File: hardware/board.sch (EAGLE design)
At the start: 45 parts, among them IC1 0915BM15A0001, J1 U.FL, U3 BLE113-A, X1 26MHz 10pF 10ppm -20C +70C, X3 MINI-USB-UX60-MB-5ST

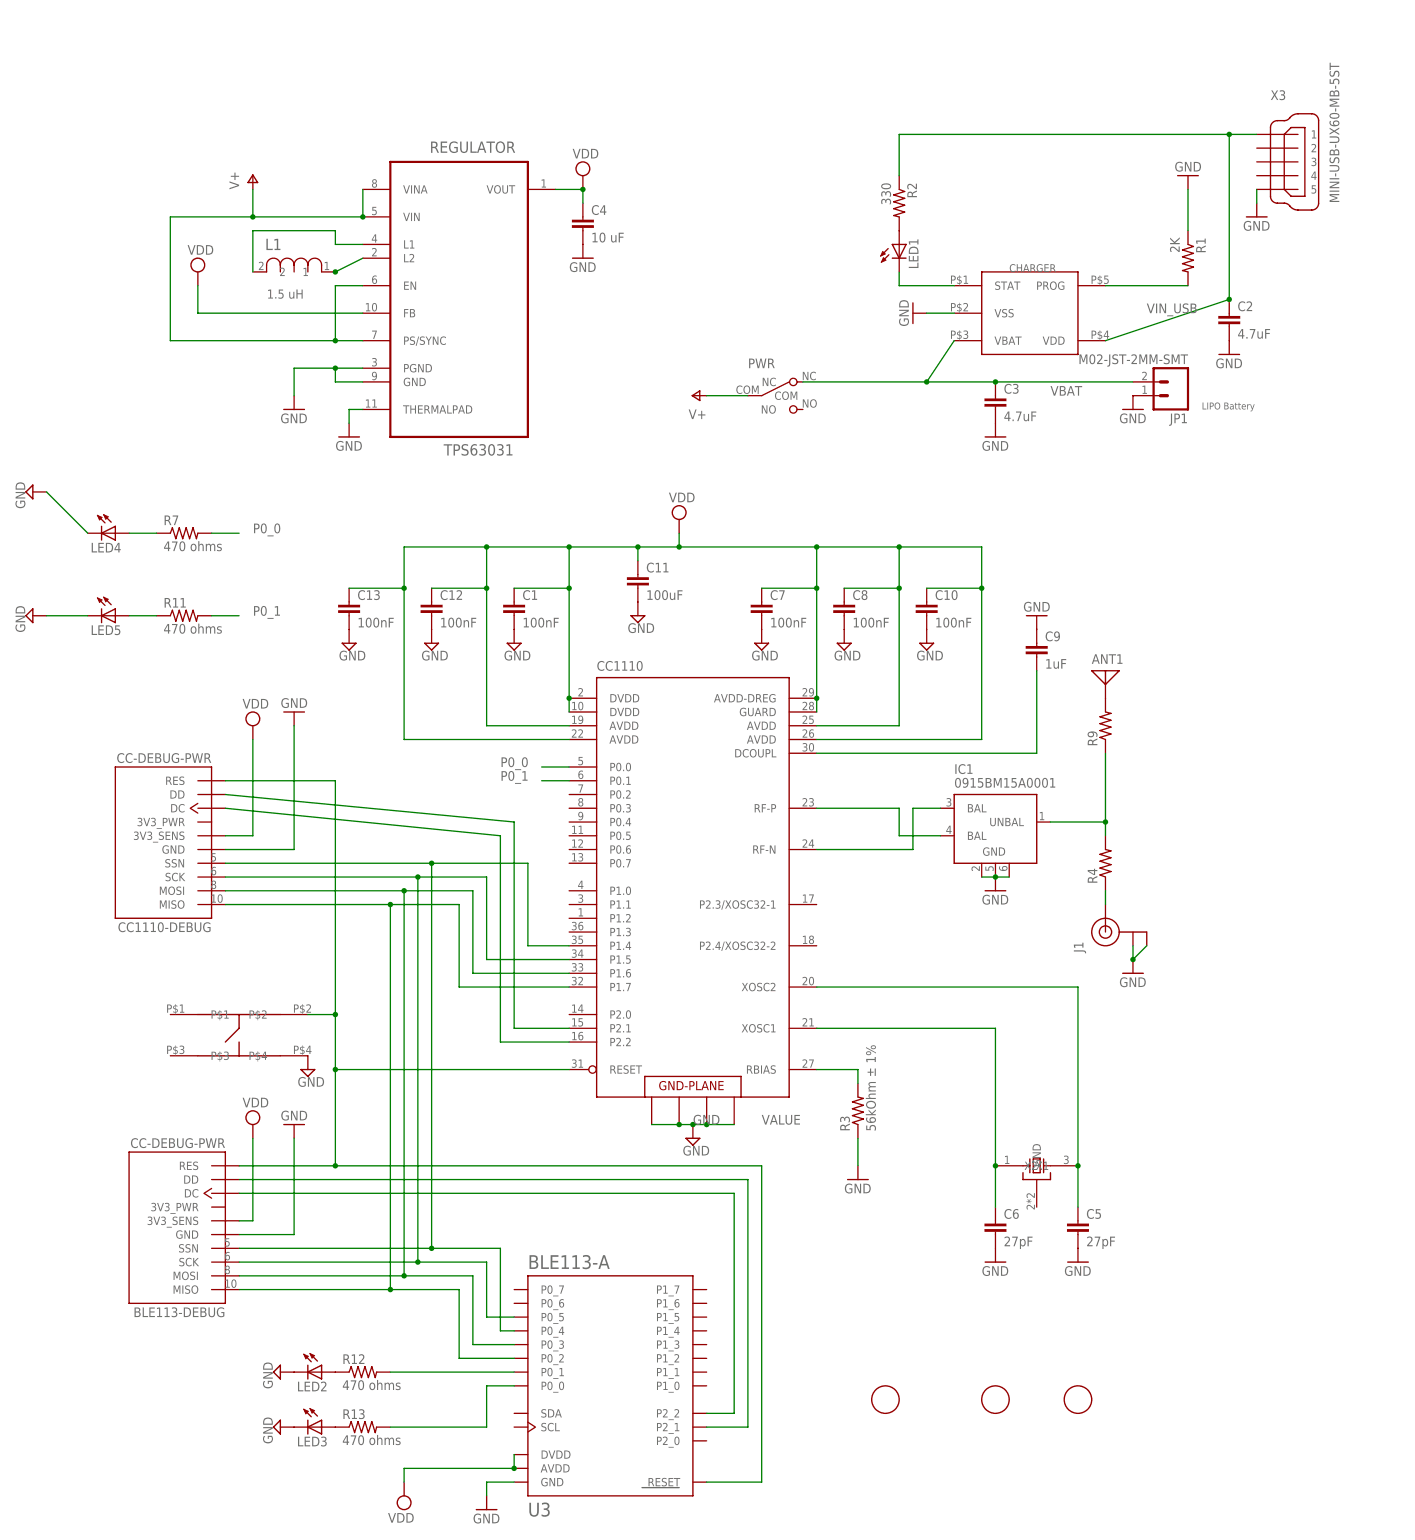
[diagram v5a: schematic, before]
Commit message: Add colors to leds, and switch 4.7uF cap from 0402 to 0603 package
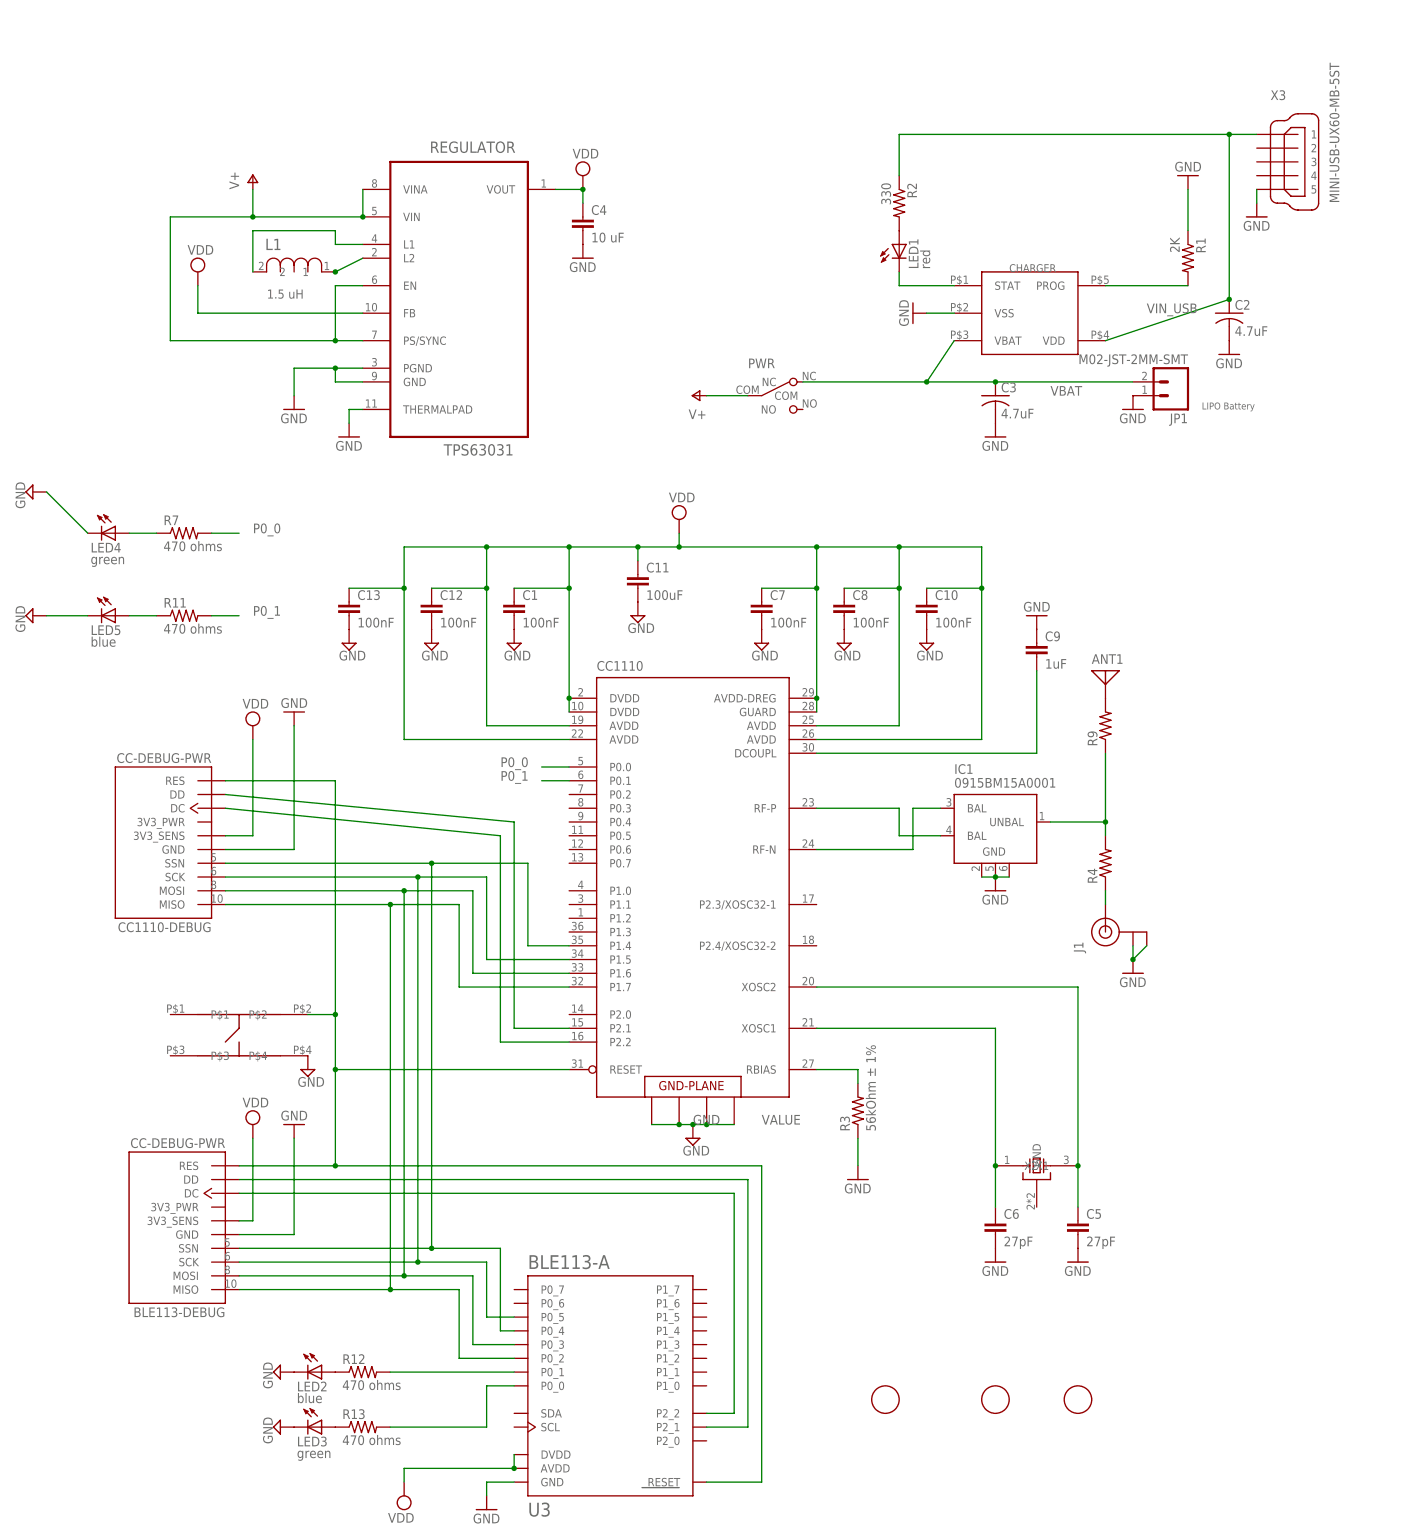
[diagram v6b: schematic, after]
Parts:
- C2: device rcl:C-EUC0402K -> rcl:C-USC0603K
- C3: device rcl:C-EUC0603K -> rcl:C-USC0603K
- LED1: value (none) -> red
- LED2, LED5: value (none) -> blue
- LED3, LED4: value (none) -> green
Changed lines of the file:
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@@
 <part name="JP1" library="SparkFun-Connectors" deviceset="M02" device="-JST-2MM-SMT"/>
 <part name="GND1" library="supply1" deviceset="GND" device=""/>
-<part name="C2" library="rcl" deviceset="C-EU" device="C0402K" value="4.7uF"/>
+<part name="C2" library="rcl" deviceset="C-US" device="C0603K" value="4.7uF"/>
 <part name="GND3" library="supply1" deviceset="GND" device=""/>
 <part name="R1" library="rcl" deviceset="R-US_" device="R0402" value="2K"/>
 <part name="R2" library="rcl" deviceset="R-US_" device="R0402" value="330"/>
-<part name="LED1" library="led" deviceset="LED" device="SML0603"/>
+<part name="LED1" library="led" deviceset="LED" device="SML0603" value="red"/>
 <part name="GND2" library="supply1" deviceset="GND" device=""/>
 <part name="GND4" library="supply1" deviceset="GND" device=""/>
-<part name="C3" library="rcl" deviceset="C-EU" device="C0603K" value="4.7uF"/>
+<part name="C3" library="rcl" deviceset="C-US" device="C0603K" value="4.7uF"/>
 <part name="GND5" library="supply1" deviceset="GND" device=""/>
 <part name="GND6" library="supply1" deviceset="GND" device=""/>
@@
 <part name="R11" library="rcl" deviceset="R-US_" device="R0402" value="470 ohms"/>
 <part name="SUPPLY10" library="supply2" deviceset="GND" device=""/>
-<part name="LED4" library="led" deviceset="LED" device="SML0603"/>
-<part name="LED5" library="led" deviceset="LED" device="SML0603"/>
+<part name="LED4" library="led" deviceset="LED" device="SML0603" value="green"/>
+<part name="LED5" library="led" deviceset="LED" device="SML0603" value="blue"/>
 <part name="SUPPLY11" library="supply2" deviceset="GND" device=""/>
 <part name="SUPPLY12" library="supply2" deviceset="GND" device=""/>
-<part name="LED2" library="led" deviceset="LED" device="SML0603"/>
+<part name="LED2" library="led" deviceset="LED" device="SML0603" value="blue"/>
 <part name="R12" library="rcl" deviceset="R-US_" device="R0402" value="470 ohms"/>
 <part name="SUPPLY13" library="supply2" deviceset="GND" device=""/>
-<part name="LED3" library="led" deviceset="LED" device="SML0603"/>
+<part name="LED3" library="led" deviceset="LED" device="SML0603" value="green"/>
 <part name="R13" library="rcl" deviceset="R-US_" device="R0402" value="470 ohms"/>
 <part name="C7" library="rcl" deviceset="C-EU" device="C0402" value="100nF"/>

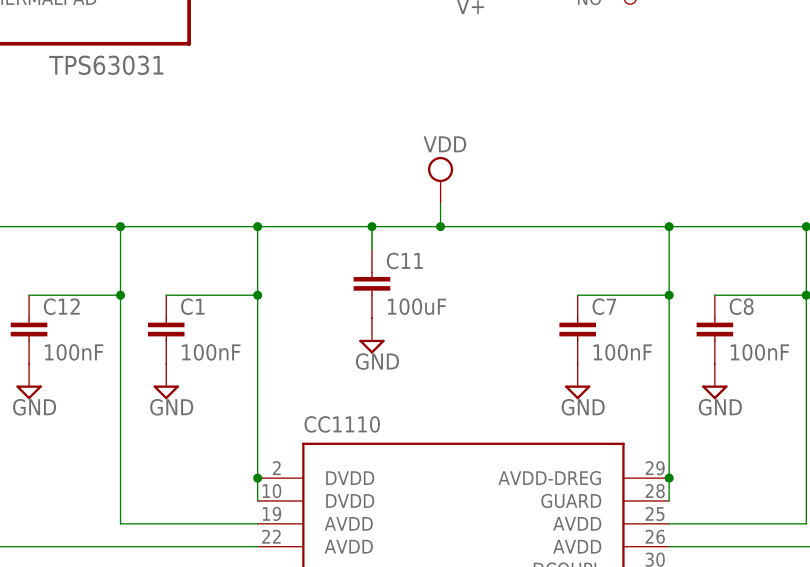
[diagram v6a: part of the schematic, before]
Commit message: Update C11 to 0805
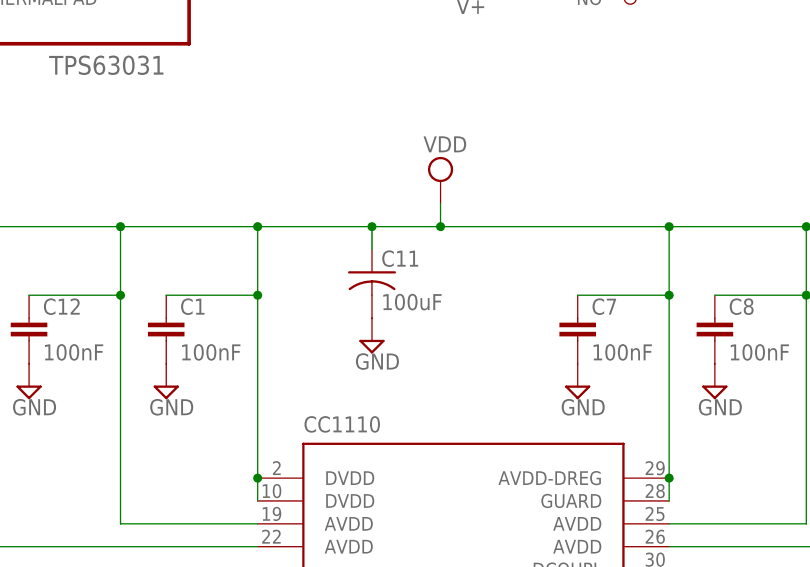
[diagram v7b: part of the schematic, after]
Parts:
- C11: device rcl:C-EUC0402 -> rcl:C-USC0805K
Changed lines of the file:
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@@
 <part name="SUPPLY19" library="supply2" deviceset="GND" device=""/>
 <part name="SUPPLY20" library="supply2" deviceset="GND" device=""/>
-<part name="C11" library="rcl" deviceset="C-EU" device="C0402" value="100uF"/>
+<part name="C11" library="rcl" deviceset="C-US" device="C0805K" value="100uF"/>
 <part name="SUPPLY15" library="supply2" deviceset="GND" device=""/>
 <part name="SUPPLY18" library="supply2" deviceset="VDD" device=""/>

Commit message: Adding cc-debugger connection illustration
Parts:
- L1: MPN (none) -> MLF1608A1R5KTD25; SUPPLIER (none) -> Mouser
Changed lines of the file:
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@@
 <part name="GND7" library="supply1" deviceset="GND" device=""/>
 <part name="GND8" library="supply1" deviceset="GND" device=""/>
-<part name="L1" library="Bourns_By_element14_Batch_1" deviceset="PM0603-R12J-RC" device="" value="1.5 uH"/>
+<part name="L1" library="Bourns_By_element14_Batch_1" deviceset="PM0603-R12J-RC" device="" value="1.5 uH">
+<attribute name="MPN" value="MLF1608A1R5KTD25"/>
+<attribute name="OC_FARNELL" value=""/>
+<attribute name="OC_NEWARK" value=""/>
+<attribute name="SUPPLIER" value="Mouser"/>
+</part>
 <part name="C4" library="rcl" deviceset="C-EU" device="C0805K" value="10 uF"/>
 <part name="GND9" library="supply1" deviceset="GND" device=""/>
